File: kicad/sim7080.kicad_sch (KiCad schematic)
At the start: 23 parts, among them J2 USB_C_SIM, J3 SIM_Card, U2 SIM7080G, U6 TXU0204PWR, U7 USBLC6-2SC6

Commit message: Draft
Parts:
- removed C20, C21, C22, C23, C31: 100nF, Capacitor_SMD:C_0603_1608Metric, symbol Device:C_Small
- removed C27: 10µF, Capacitor_SMD:C_0603_1608Metric, symbol Device:C_Small
- removed C29, C30: 100µF, Capacitor_SMD:C_1206_3216Metric, symbol Device:C_Small
- removed D2: ESD5Z3.3T1G, Diode_SMD:D_SOD-523, symbol Diode:ESD5Zxx
- removed D3: ESDA6V1W5, lpwa-node:SOT65P210X110-5N, symbol lpwa-node:ESDA6V1W5
- removed J2: USB_C_SIM, lpwa-node:USB_C_Receptacle_HRO_TYPE-C-31-M-12, symbol Connector:USB_C_Receptacle_USB2.0
- removed J3: SIM_Card, lpwa-node:SMN-304, symbol Connector:SIM_Card_Shielded
- removed JP1: SIM USB VBUS, symbol Jumper:Jumper_2_Small_Bridged
- removed R7, R8: 5.1k, Resistor_SMD:R_0603_1608Metric, symbol Device:R_Small
- removed R9: 22R, symbol Device:R_Small
- removed U2: SIM7080G, lpwa-node:SIM7080G, symbol lpwa-node:SIM7080G
- removed U6: TXU0204PWR, lpwa-node:SOP65P640X120-14N, symbol lpwa-node:TXU0204PWR
- removed U7: USBLC6-2SC6, Package_TO_SOT_SMD:SOT-23-6, symbol Power_Protection:USBLC6-2SC6
- added C10: 10µF, Capacitor_SMD:C_0603_1608Metric, symbol Device:C_Small
- added C11, C13: 100µF, Capacitor_SMD:C_1206_3216Metric, symbol Device:C_Small
- added C12, C14, C15, C8, C9: 100nF, Capacitor_SMD:C_0603_1608Metric, symbol Device:C_Small
- added D4: ESD5Z3.3T1G, Diode_SMD:D_SOD-523, symbol Diode:ESD5Zxx
- added D5: ESDA6V1W5, lpwa-node:SOT65P210X110-5N, symbol lpwa-node:ESDA6V1W5
- added J4: USB_C_SIM, lpwa-node:USB_C_Receptacle_HRO_TYPE-C-31-M-12, symbol Connector:USB_C_Receptacle_USB2.0
- added J5: SIM_Card, lpwa-node:SMN-304, symbol Connector:SIM_Card_Shielded
- added JP10: SIM USB VBUS, lpwa-node:SolderJumper-2_P1.3mm_Bridged_RoundedPad1.0x1.5mm, symbol Jumper:Jumper_2_Small_Bridged
- added JP2: ESP_TXD, lpwa-node:SolderJumper-2_P1.3mm_Bridged_RoundedPad1.0x1.5mm, symbol Jumper:Jumper_2_Small_Bridged
- added JP3: ESP_DTR, lpwa-node:SolderJumper-2_P1.3mm_Bridged_RoundedPad1.0x1.5mm, symbol Jumper:Jumper_2_Small_Bridged
- added JP4: ESP_RXD, lpwa-node:SolderJumper-2_P1.3mm_Bridged_RoundedPad1.0x1.5mm, symbol Jumper:Jumper_2_Small_Bridged
- added JP5: ESP_STATUS, lpwa-node:SolderJumper-2_P1.3mm_Bridged_RoundedPad1.0x1.5mm, symbol Jumper:Jumper_2_Small_Bridged
- added JP6: SIM_STATUS, lpwa-node:SolderJumper-2_P1.3mm_Bridged_RoundedPad1.0x1.5mm, symbol Jumper:Jumper_2_Small_Bridged
- added JP7: SIM_TXD, lpwa-node:SolderJumper-2_P1.3mm_Bridged_RoundedPad1.0x1.5mm, symbol Jumper:Jumper_2_Small_Bridged
- added JP8: SIM_DTR, lpwa-node:SolderJumper-2_P1.3mm_Bridged_RoundedPad1.0x1.5mm, symbol Jumper:Jumper_2_Small_Bridged
- added JP9: SIM_RXD, lpwa-node:SolderJumper-2_P1.3mm_Bridged_RoundedPad1.0x1.5mm, symbol Jumper:Jumper_2_Small_Bridged
- added R12: 22R, Resistor_SMD:R_0603_1608Metric, symbol Device:R_Small
- added R13, R14: 5.1k, Resistor_SMD:R_0603_1608Metric, symbol Device:R_Small
- added TP1: CTS, TestPoint:TestPoint_Pad_D1.5mm, symbol Connector:TestPoint_Small
- added TP2: RTS, TestPoint:TestPoint_Pad_D1.5mm, symbol Connector:TestPoint_Small
- added U6: SIM7080G, lpwa-node:SIM7080G, symbol lpwa-node:SIM7080G
- added U7: TXU0204PWR, lpwa-node:SOP65P640X120-14N, symbol lpwa-node:TXU0204PWR
- added U8: USBLC6-2SC6, Package_TO_SOT_SMD:SOT-23-6, symbol Power_Protection:USBLC6-2SC6
- R10, R11: footprint (none) -> Resistor_SMD:R_0603_1608Metric; LCSC Part # (none) -> C23345
- TP3: value CTS -> ESP_SIM_RI; footprint (none) -> TestPoint:TestPoint_Pad_D1.5mm
- TP4: value RTS -> RI; footprint (none) -> TestPoint:TestPoint_Pad_D1.5mm
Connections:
- net +BATT: now also C10.2, C11.2, C13.2, C8.2, U6.34 (VBAT), U6.35 (VBAT)
- net D+: now also J4.A6 (D+), J4.B6 (D+), U8.3 (I/O2)
- net D-: now also J4.A7 (D-), J4.B7 (D-), U8.1 (I/O1)
- net ESP_DTR: now also JP3.1 (A)
- net ESP_RXD: now also JP4.1 (A)
- net ESP_SIM_RI: now also TP3.1
- net ESP_TXD: now also JP2.1 (A)
- net GND: now also C10.1, C11.1, C12.1, C13.1, C14.1, C15.1, C8.1, C9.1, D4.2 (A), D5.2, J4.A1 (GND), J4.A12 (GND), J4.B1 (GND), J4.B12 (GND), J4.S1 (SHIELD), J5.5 (GND), J5.SH, R13.2, R14.1, U6.13 (GND), U6.19 (GND), U6.21 (GND), U6.27 (GND), U6.30 (GND), U6.31 (GND), U6.33 (GND), U6.36 (GND), U6.37 (GND), U6.45 (GND), U6.63 (GND), U6.66 (GND), U6.67 (GND), U6.69 (GND), U6.70 (GND), U6.71 (GND), U6.72 (GND), U6.73 (GND), U6.74 (GND), U6.75 (GND), U6.76 (GND), U6.77 (GND), U6.8 (GND), U7.7 (GND), U8.2 (GND)
- net SIM_DTR: now also JP8.2 (B), U6.6 (UART1_DTR)
- net SIM_GNSS_ANT: now also U6.68 (GNSS_ANT)
- net SIM_LTE_ANT: now also U6.32 (RF_ANT)
- net SIM_PWRKEY: now also D4.1 (K), U6.39 (PWRKEY)
- net SIM_RI: now also TP4.1, U6.7 (UART1_RI)
- net SIM_RXD: now also JP9.2 (B), U6.2 (UART1_RXD)
- net SIM_SIM_CLK: now also U6.16 (SIM_CLK)
- net SIM_SIM_DATA: now also U6.15 (SIM_DATA)
- net SIM_SIM_RST: now also R12.1, U6.17 (SIM_RST)
- net SIM_SIM_VDD: now also C14.2, D5.1, J5.1 (VCC), U6.18 (SIM_VDD)
- net SIM_TXD: now also JP7.2 (B), U6.1 (UART1_TXD)
- net SIM_USB_D+: now also U6.25 (USB_DP), U8.4 (I/O2)
- net SIM_USB_D-: now also U6.26 (USB_DM), U8.6 (I/O1)
- net USB_SIM_+5V: now also JP10.2 (B), U6.24 (USB_VBUS)
- net VDD_SIM_EXT: now also C12.2, U6.40 (VDD_EXT), U7.14 (VCCB)
- net at R11.2: now also D5.3, J5.7 (I/O)
- net at R10.2: now also D5.4, J5.3 (CLK)
- new net: TP1.1, U6.4 (UART1_CTS)
- new net: TP2.1, U6.3 (UART1_RTS)
- new net: JP9.1 (A), U7.13 (B1Y)
- new net: JP4.2 (B), U7.4 (A3Y)
- new net: JP6.1 (A), U7.10 (B4)
- new net: JP7.1 (A), U7.11 (B3)
- new net: JP8.1 (A), U7.12 (B2Y)
- new net: JP2.2 (B), U7.2 (A1)
- new net: JP3.2 (B), U7.3 (A2)
- new net: JP5.2 (B), U7.5 (A4Y)
- new net: U7.6 (NC), U7.9 (NC)
- new net: J4.B5 (CC2), R14.2
- new net: D5.5, J5.2 (RST), R12.2
- new net: J4.A5 (CC1), R13.1
- new net +3V3: C9.2, U7.1 (VCCA), U7.8 (OE)
- new net ESP_SIM_STATUS: JP5.1 (A)
- new net SIM_STATUS: JP6.2 (B), U6.42 (STATUS)
- new net SIM_USB_VBUS: C15.2, J4.A4 (VBUS), J4.A9 (VBUS), J4.B4 (VBUS), J4.B9 (VBUS), JP10.1 (A), U8.5 (VBUS)

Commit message: Draft
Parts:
- JP10: value SIM USB VBUS -> SIM_USB_VBUS
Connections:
- net +3V3 renamed 3V0
- net +BATT renamed VBAT
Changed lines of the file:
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@@
 			)
 		)
-		(property "Value" "+3V3"
-			(at 115.57 22.86 0)
+		(property "Value" "3V0"
+			(at 118.11 26.6699 0)
 			(show_name no)
 			(do_not_autoplace no)
@@
 					(size 1.27 1.27)
 				)
+				(justify left)
 			)
 		)
@@
 			)
 		)
-		(property "Value" "+3V3"
+		(property "Value" "3V0"
 			(at 142.24 66.04 0)
 			(show_name no)
@@
 			)
 		)
-		(property "Value" "+3V3"
+		(property "Value" "3V0"
 			(at 73.66 27.94 0)
 			(show_name no)
@@
 			)
 		)
-		(property "Value" "SIM USB VBUS"
+		(property "Value" "SIM_USB_VBUS"
 			(at 256.54 110.49 0)
 			(show_name no)
@@
 			)
 		)
-		(property "Value" "+BATT"
+		(property "Value" "VSYS"
 			(at 175.26 100.3299 90)
 			(show_name no)

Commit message: Draft
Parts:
- removed TP3: ESP_SIM_RI, TestPoint:TestPoint_Pad_D1.5mm, symbol Connector:TestPoint_Small
- added C22: 100µF, Capacitor_SMD:C_1206_3216Metric, symbol Device:C_Small
- added TP13: PWRKEY, TestPoint:TestPoint_Pad_D1.5mm, symbol Connector:TestPoint_Small
- added TP14: STATUS, TestPoint:TestPoint_Pad_D1.5mm, symbol Connector:TestPoint_Small
- added TP15: NETLIGHT, TestPoint:TestPoint_Pad_D1.5mm, symbol Connector:TestPoint_Small
- C11, C13: LCSC Part # C178304 -> C7432784
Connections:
- net GND: now also C22.1
- net SIM_PWRKEY: now also TP13.1
- net SIM_STATUS: now also TP14.1
- net VBAT: now also C22.2
- net at U6.41 (NETLIGHT): now also TP15.1
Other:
- moved on the sheet: C10, C11, C13, C8, D4

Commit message: First orderable version
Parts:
- added R22: 10k, Resistor_SMD:R_0603_1608Metric, symbol Device:R_Small
- J4: symbol Connector:USB_C_Receptacle_USB2.0 -> Connector:USB_C_Receptacle_USB2.0_16P
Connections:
- net GND: now also J4.SH (SHIELD); no longer J4.S1 (SHIELD)
- net SIM_PWRKEY: now also R22.1; no longer D4.1 (K), TP13.1, U6.39 (PWRKEY)
- new net: D4.1 (K), R22.2, TP13.1, U6.39 (PWRKEY)
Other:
- moved on the sheet: D4, TP13
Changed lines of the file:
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@@
 	)
 	(junction
-		(at 48.26 105.41)
-		(diameter 0)
-		(color 0 0 0 0)
-	)
-	(junction
 		(at 107.95 113.03)
 		(diameter 0)
@@
 	)
 	(junction
+		(at 48.26 105.41)
+		(diameter 0)
+		(color 0 0 0 0)
+	)
+	(junction
 		(at 248.92 34.29)
 		(diameter 0)
@@
 	)
 	(junction
-		(at 41.91 99.06)
+		(at 41.91 93.98)
 		(diameter 0)
 		(color 0 0 0 0)
@@
 	(wire
 		(pts
-			(xy 41.91 99.06) (xy 48.26 99.06)
+			(xy 41.91 93.98) (xy 48.26 93.98)
 		)
 		(stroke
@@
 	(wire
 		(pts
-			(xy 45.72 105.41) (xy 48.26 105.41)
+			(xy 35.56 105.41) (xy 40.64 105.41)
 		)
 		(stroke
@@
 	(wire
 		(pts
+			(xy 45.72 105.41) (xy 48.26 105.41)
+		)
+		(stroke
+			(width 0)
+			(type default)
+		)
+	)
+	(wire
+		(pts
 			(xy 116.84 58.42) (xy 116.84 60.96)
 		)
@@
 	(wire
 		(pts
-			(xy 48.26 99.06) (xy 48.26 105.41)
+			(xy 48.26 93.98) (xy 48.26 105.41)
 		)
 		(stroke
@@
 	(wire
 		(pts
-			(xy 22.86 99.06) (xy 27.94 99.06)
+			(xy 22.86 93.98) (xy 27.94 93.98)
 		)
 		(stroke
@@
 	(wire
 		(pts
-			(xy 35.56 99.06) (xy 41.91 99.06)
+			(xy 35.56 93.98) (xy 41.91 93.98)
 		)
 		(stroke
@@
 	(wire
 		(pts
-			(xy 41.91 96.52) (xy 41.91 99.06)
+			(xy 41.91 91.44) (xy 41.91 93.98)
 		)
 		(stroke
@@
 	(wire
 		(pts
-			(xy 22.86 100.33) (xy 22.86 99.06)
+			(xy 22.86 95.25) (xy 22.86 93.98)
 		)
 		(stroke
@@
 	(global_label "SIM_PWRKEY"
 		(shape input)
-		(at 45.72 105.41 180)
+		(at 35.56 105.41 180)
 		(fields_autoplaced yes)
 		(effects
@@
 		)
 		(property "Intersheetrefs" "${INTERSHEET_REFS}"
-			(at 31.0025 105.41 0)
+			(at 20.8425 105.41 0)
 			(hide yes)
 			(show_name no)
@@
 	(symbol
 		(lib_id "power:GND")
-		(at 22.86 100.33 0)
+		(at 22.86 95.25 0)
 		(unit 1)
 		(body_style 1)
@@
 		(fields_autoplaced yes)
 		(property "Reference" "#PWR031"
-			(at 22.86 106.68 0)
+			(at 22.86 101.6 0)
 			(hide yes)
 			(show_name no)
@@
 		)
 		(property "Value" "GND"
-			(at 22.86 105.41 0)
+			(at 22.86 100.33 0)
 			(show_name no)
 			(do_not_autoplace no)
@@
 		)
 		(property "Footprint" ""
-			(at 22.86 100.33 0)
+			(at 22.86 95.25 0)
 			(hide yes)
 			(show_name no)
@@
 		)
 		(property "Datasheet" ""
-			(at 22.86 100.33 0)
+			(at 22.86 95.25 0)
 			(hide yes)
 			(show_name no)
@@
 		)
 		(property "Description" "Power symbol creates a global label with name \"GND\" , ground"
-			(at 22.86 100.33 0)
+			(at 22.86 95.25 0)
 			(hide yes)
 			(show_name no)
@@
 	(symbol
 		(lib_id "Diode:ESD5Zxx")
-		(at 31.75 99.06 180)
+		(at 31.75 93.98 180)
 		(unit 1)
 		(body_style 1)
@@
 		(fields_autoplaced yes)
 		(property "Reference" "D4"
-			(at 31.75 92.71 0)
+			(at 31.75 87.63 0)
 			(show_name no)
 			(do_not_autoplace no)
@@
 		)
 		(property "Value" "ESD5Z3.3T1G"
-			(at 31.75 95.25 0)
+			(at 31.75 90.17 0)
 			(show_name no)
 			(do_not_autoplace no)
@@
 		)
 		(property "Footprint" "Diode_SMD:D_SOD-523"
-			(at 31.75 94.615 0)
+			(at 31.75 89.535 0)
 			(hide yes)
 			(show_name no)
@@
 		)
 		(property "Datasheet" "https://www.onsemi.com/pdf/datasheet/esd5z2.5t1-d.pdf"
-			(at 31.75 99.06 0)
+			(at 31.75 93.98 0)
 			(hide yes)
 			(show_name no)
@@
 		)
 		(property "Description" "ESD Protection Diode, SOD-523"
-			(at 31.75 99.06 0)
+			(at 31.75 93.98 0)
 			(hide yes)
 			(show_name no)
@@
 	(symbol
 		(lib_id "Connector:TestPoint_Small")
-		(at 41.91 96.52 0)
+		(at 41.91 91.44 0)
 		(unit 1)
 		(body_style 1)
@@
 		(fields_autoplaced yes)
 		(property "Reference" "TP13"
-			(at 43.18 95.2499 0)
+			(at 43.18 90.1699 0)
 			(show_name no)
 			(do_not_autoplace no)
@@
 		)
 		(property "Value" "PWRKEY"
-			(at 43.18 97.7899 0)
+			(at 43.18 92.7099 0)
 			(show_name no)
 			(do_not_autoplace no)
@@
 		)
 		(property "Footprint" "TestPoint:TestPoint_Pad_D1.5mm"
-			(at 46.99 96.52 0)
+			(at 46.99 91.44 0)
 			(hide yes)
 			(show_name no)
@@
 		)
 		(property "Datasheet" ""
-			(at 46.99 96.52 0)
+			(at 46.99 91.44 0)
 			(hide yes)
 			(show_name no)
@@
 		)
 		(property "Description" "test point"
-			(at 41.91 96.52 0)
+			(at 41.91 91.44 0)
 			(hide yes)
 			(show_name no)
@@
 	)
 	(symbol
+		(lib_id "Device:R_Small")
+		(at 43.18 105.41 90)
+		(unit 1)
+		(body_style 1)
+		(exclude_from_sim no)
+		(in_bom yes)
+		(on_board yes)
+		(in_pos_files yes)
+		(dnp no)
+		(fields_autoplaced yes)
+		(property "Reference" "R22"
+			(at 43.18 100.33 90)
+			(show_name no)
+			(do_not_autoplace no)
+			(effects
+				(font
+					(size 1.27 1.27)
+				)
+			)
+		)
+		(property "Value" "10k"
+			(at 43.18 102.87 90)
+			(show_name no)
+			(do_not_autoplace no)
+			(effects
+				(font
+					(size 1.27 1.27)
+				)
+			)
+		)
+		(property "Footprint" "Resistor_SMD:R_0603_1608Metric"
+			(at 43.18 105.41 0)
+			(hide yes)
+			(show_name no)
+			(do_not_autoplace no)
+			(effects
+				(font
+					(size 1.27 1.27)
+				)
+			)
+		)
+		(property "Datasheet" ""
+			(at 43.18 105.41 0)
+			(hide yes)
+			(show_name no)
+			(do_not_autoplace no)
+			(effects
+				(font
+					(size 1.27 1.27)
+				)
+			)
+		)
+		(property "Description" "Resistor, small symbol"
+			(at 43.18 105.41 0)
+			(hide yes)
+			(show_name no)
+			(do_not_autoplace no)
+			(effects
+				(font
+					(size 1.27 1.27)
+				)
+			)
+		)
+		(property "LCSC Part #" "C25804"
+			(at 43.18 105.41 0)
+			(hide yes)
+			(show_name no)
+			(do_not_autoplace no)
+			(effects
+				(font
+					(size 1.27 1.27)
+				)
+			)
+		)
+		(pin "1"
+		)
+		(pin "2"
+		)
+		(instances
+			(project "lpwa-node"
+				(path "/befb51be-ef91-4a91-a5d6-0f5d1fe0ec19/7413c64b-a7f8-4524-b57e-98dbe08fecb0"
+					(reference "R22")
+					(unit 1)
+				)
+			)
+		)
+	)
+	(symbol
 		(lib_id "Device:C_Small")
 		(at 153.67 73.66 180)
@@
 	)
 	(symbol
-		(lib_id "Connector:USB_C_Receptacle_USB2.0")
+		(lib_id "Connector:USB_C_Receptacle_USB2.0_16P")
 		(at 209.55 128.27 0)
 		(unit 1)
@@
 			)
 		)
-		(property "Description" ""
+		(property "Description" "USB 2.0-only 16P Type-C Receptacle connector"
 			(at 209.55 128.27 0)
 			(hide yes)
@@
 		(pin "B9"
 		)
-		(pin "S1"
+		(pin "SH"
 		)
 		(instances

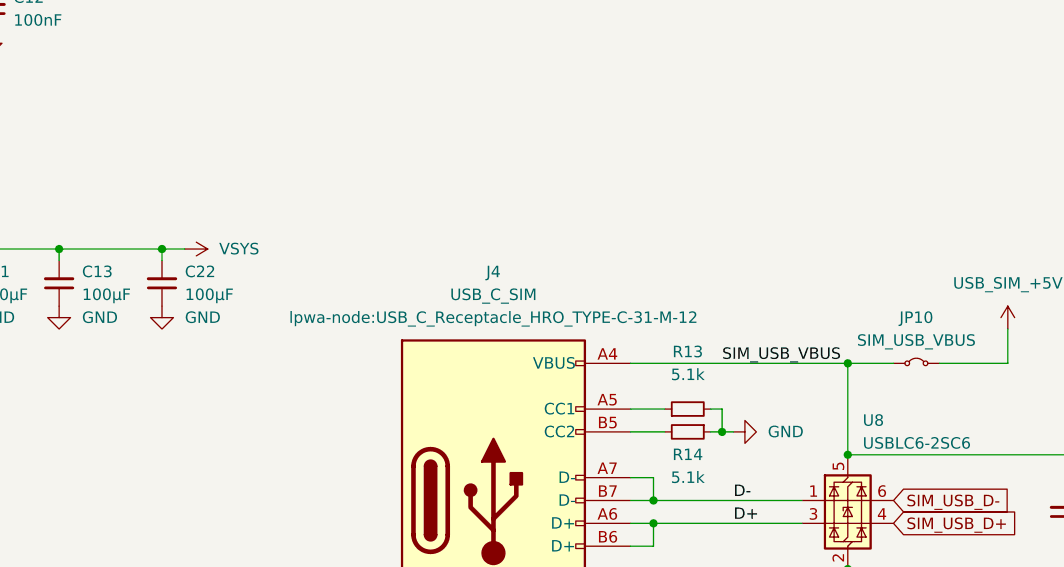
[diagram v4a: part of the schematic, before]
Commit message: Optimize for manufacturing, add part numbers
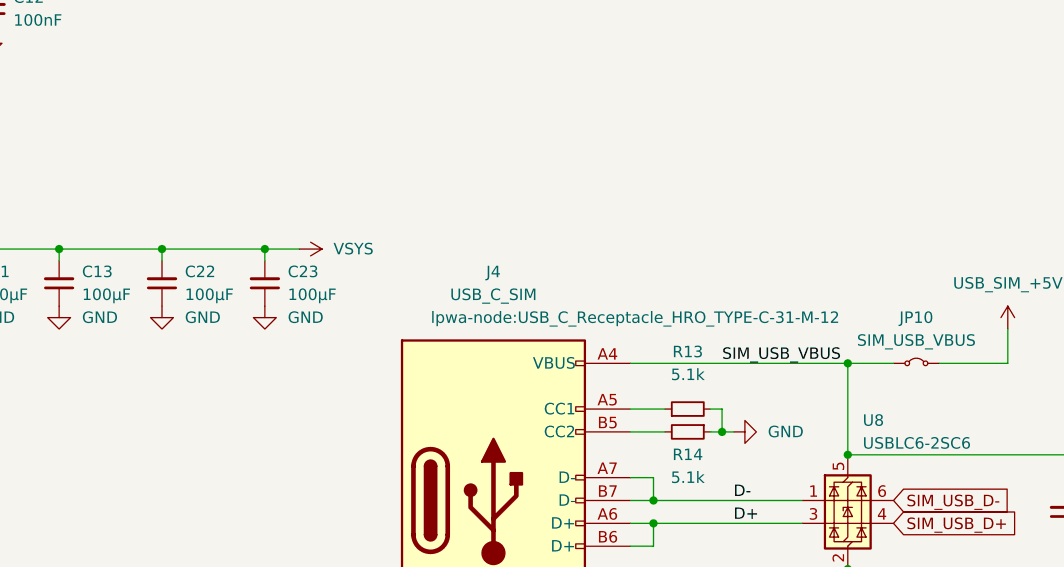
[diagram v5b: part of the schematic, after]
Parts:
- added C23: 100µF, Capacitor_SMD:C_1206_3216Metric, symbol Device:C_Small
- C12, C14, C15, C8, C9: LCSC Part # C14663 -> C161115
- D4: LCSC Part # (none) -> C61148
- JP10, JP2, JP3, JP4, JP5, JP6, JP7, JP8, JP9, TP14, TP15, TP4: now left out of the parts list
- U6: LCSC Part # (none) -> C18548266
- U7: Check_prices https://www.snapeda.com/parts/TXU0104PWR/Texas+Instruments/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 -> (none); MP TXU0104PWR -> (none); SnapEDA_Link https://www.snapeda.com/parts/TXU0104PWR/Texas+Instruments/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 -> (none)
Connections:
- net GND: now also C23.1
- net VBAT: now also C23.2

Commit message: Release A
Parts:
- J4, TP1, TP13, TP2: now left out of the parts list
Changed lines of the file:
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@@
 		(body_style 1)
 		(exclude_from_sim no)
-		(in_bom yes)
+		(in_bom no)
 		(on_board yes)
-		(in_pos_files yes)
+		(in_pos_files no)
 		(dnp no)
 		(fields_autoplaced yes)
@@
 		(body_style 1)
 		(exclude_from_sim no)
-		(in_bom yes)
+		(in_bom no)
 		(on_board yes)
-		(in_pos_files yes)
+		(in_pos_files no)
 		(dnp no)
 		(fields_autoplaced yes)
@@
 		(body_style 1)
 		(exclude_from_sim no)
-		(in_bom yes)
+		(in_bom no)
 		(on_board yes)
-		(in_pos_files yes)
+		(in_pos_files no)
 		(dnp no)
 		(fields_autoplaced yes)
@@
 		(body_style 1)
 		(exclude_from_sim no)
-		(in_bom yes)
+		(in_bom no)
 		(on_board yes)
-		(in_pos_files yes)
+		(in_pos_files no)
 		(dnp no)
 		(property "Reference" "J4"
